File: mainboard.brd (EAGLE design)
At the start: 96.5 x 29.2 mm, 20 parts, among them IC1 LF353D, J1 AUDIO-JACKERTHENVAR, J2 AUDIO-JACKERTHENVAR, J3 AUDIO-JACKERTHENVAR, J4 AUDIO-JACKERTHENVAR, J5 AUDIO-JACKERTHENVAR, J6 POWER_SIMPLE10, P1 100KB, P2 100KB, P3 100KB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

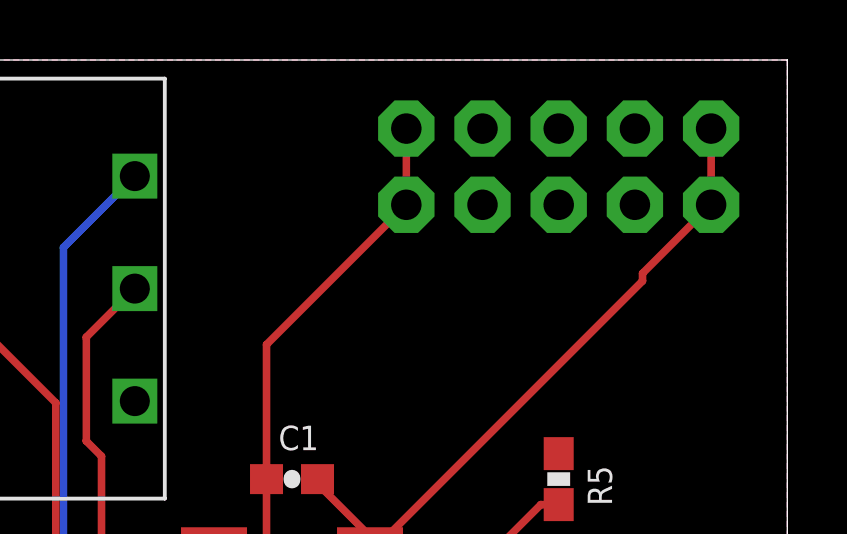
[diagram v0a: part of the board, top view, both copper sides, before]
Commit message: Switched to 16 pin connector.
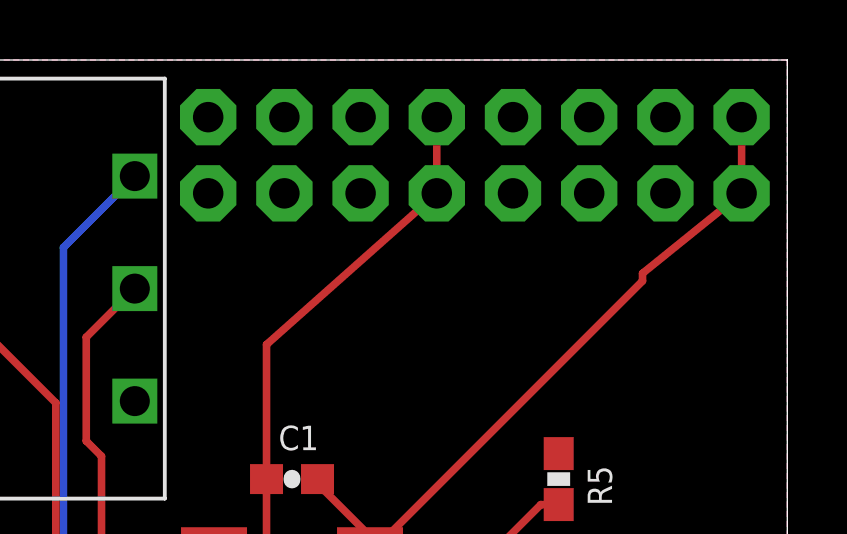
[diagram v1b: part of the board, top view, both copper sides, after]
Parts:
- J6: value POWER_SIMPLE10 -> POWER_SIMPLE16; device eurorack:POWER_10 -> eurorack:POWER_16
- moved J6 0.46 mm to (88.6, 26.0)
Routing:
- net -12V: track 21.3 -> 22.3 mm
- net +12V: track 20.8 -> 21.8 mm
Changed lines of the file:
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@@
 <attribute name="VALUE" x="81.915" y="15.367" size="1.27" layer="27" rot="R180"/>
 </element>
-<element name="J6" library="eurorack" package="POWER_10" value="POWER_SIMPLE10" x="88.9" y="25.654" smashed="yes" rot="MR0">
-<attribute name="NAME" x="85.09" y="21.209" size="1.27" layer="26" ratio="10" rot="MR0"/>
+<element name="J6" library="eurorack" package="POWER_16" value="POWER_SIMPLE16" x="88.646" y="26.035" smashed="yes" rot="MR0">
+<attribute name="NAME" x="84.836" y="21.59" size="1.27" layer="26" ratio="10" rot="MR0"/>
 </element>
 <element name="J1" library="erthenvar" package="ERTHENVAR-JACK" value="AUDIO-JACKERTHENVAR" x="7.62" y="7.62" smashed="yes" rot="R180">
@@
 <contactref element="IC1" pad="4"/>
 <contactref element="C1" pad="1"/>
-<wire x1="93.98" y1="24.384" x2="93.98" y2="26.924" width="0.254" layer="1"/>
+<wire x1="94.996" y1="24.765" x2="94.996" y2="27.305" width="0.254" layer="1"/>
 <wire x1="80.86" y1="15.24" x2="80.86" y2="15.085" width="0.254" layer="1"/>
 <wire x1="80.86" y1="15.085" x2="82.61" y2="13.335" width="0.254" layer="1"/>
@@
 <wire x1="83.185" y1="13.335" x2="91.694" y2="21.844" width="0.254" layer="1"/>
 <wire x1="91.694" y1="21.844" x2="91.694" y2="22.098" width="0.254" layer="1"/>
-<wire x1="91.694" y1="22.098" x2="93.98" y2="24.384" width="0.254" layer="1"/>
+<wire x1="91.694" y1="22.098" x2="94.996" y2="24.765" width="0.254" layer="1"/>
 </signal>
 <signal name="+12V">
@@
 <contactref element="IC1" pad="8"/>
 <contactref element="C1" pad="2"/>
-<wire x1="83.82" y1="24.384" x2="83.82" y2="26.924" width="0.254" layer="1"/>
+<wire x1="84.836" y1="24.765" x2="84.836" y2="27.305" width="0.254" layer="1"/>
 <wire x1="79.16" y1="15.24" x2="79.16" y2="10.072" width="0.254" layer="1"/>
 <wire x1="79.16" y1="10.072" x2="78.74" y2="9.652" width="0.254" layer="1"/>
@@
 <wire x1="77.537" y1="9.652" x2="77.41" y2="9.525" width="0.254" layer="1"/>
 <wire x1="79.16" y1="15.24" x2="79.16" y2="19.724" width="0.254" layer="1"/>
-<wire x1="79.16" y1="19.724" x2="83.82" y2="24.384" width="0.254" layer="1"/>
+<wire x1="79.16" y1="19.724" x2="84.836" y2="24.765" width="0.254" layer="1"/>
 </signal>
 <signal name="N$1">

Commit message: @brendan0powers helped me fix the schem/board
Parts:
- added R10: 1K, SparkFun-Resistors:0603-RES
- added R8: 51K, SparkFun-Resistors:0603-RES
- added R9: 100K, SparkFun-Resistors:0603-RES
- R7: value 1K -> 100K
- moved R6 16.2 mm to (91.4, 14.0)
- moved R7 14.3 mm to (82.5, 17.8)
- moved R1 13.0 mm to (78.7, 14.0)
- moved R2 13.0 mm to (78.7, 16.5)
- moved R3 13.0 mm to (78.7, 19.1)
- moved R4 12.5 mm to (78.7, 21.6), turned to 0 degrees
- moved C1 12.0 mm to (90.2, 21.6)
- moved IC1 12.0 mm to (90.2, 17.8)
- moved R5 6.84 mm to (95.2, 17.8), turned to 270 degrees
- moved U$1 2.54 mm to (91.2, 19.1)
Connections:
- new net N$12: IC1.7, R10.1, R9.2
- new net N$14: IC1.6, R7.2, R9.1
- new net N$15: IC1.5, R8.2
- net GND: now also R8.1; no longer IC1.5
- net N$3: now also R10.2; no longer R7.2
- net N$8: no longer IC1.6, IC1.7
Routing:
- net N$12: track 0.00 -> 14.6 mm, vias 0 -> 2
- net N$8: track 26.5 -> 15.7 mm
- net -12V: track 22.3 -> 11.8 mm
- net N$10: track 11.5 -> 3.12 mm
- net N$7: track 31.2 -> 23.2 mm
- net +12V: track 21.8 -> 16.1 mm
- net N$14: track 0.00 -> 5.11 mm
- net N$4: track 68.5 -> 63.4 mm
- net N$9: track 7.36 -> 2.57 mm
- net N$11: track 19.9 -> 23.4 mm
- net N$5: track 46.0 -> 43.3 mm
- net N$15: track 0.00 -> 2.05 mm
- net N$6: vias 0 -> 2
- net N$2: vias 0 -> 2
- net N$1: vias 0 -> 2

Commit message: fix for silkscreen
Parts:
- moved U$1 10.9 mm to (81.0, 15.2)
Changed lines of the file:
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@@
 <setting verticaltext="up"/>
 </settings>
-<grid distance="0.005" unitdist="inch" unit="inch" style="lines" multiple="1" display="yes" altdistance="0.005" altunitdist="inch" altunit="inch"/>
+<grid distance="0.05" unitdist="inch" unit="inch" style="lines" multiple="1" display="yes" altdistance="0.005" altunitdist="inch" altunit="inch"/>
 <layers>
-<layer number="1" name="Top" color="4" fill="1" visible="yes" active="yes"/>
+<layer number="1" name="Top" color="4" fill="1" visible="no" active="yes"/>
 <layer number="16" name="Bottom" color="1" fill="1" visible="yes" active="yes"/>
 <layer number="17" name="Pads" color="2" fill="1" visible="yes" active="yes"/>
@@
 <wire x1="96.52" y1="0" x2="96.52" y2="29.21" width="0" layer="20"/>
 <wire x1="96.52" y1="29.21" x2="0" y2="29.21" width="0" layer="20"/>
-<text x="15.24" y="26.416" size="1.6764" layer="22" font="vector" ratio="15" rot="MR0">Manual</text>
-<text x="15.24" y="24.13" size="1.6764" layer="22" font="vector" ratio="15" rot="MR0">Mixing</text>
-<text x="15.24" y="22.098" size="1.6764" layer="22" font="vector" ratio="15" rot="MR0">Utility</text>
-<text x="15.24" y="20.066" size="1.6764" layer="22" font="vector" ratio="15" rot="MR0">Alpha</text>
+<text x="81.28" y="9.906" size="1.6764" layer="22" font="vector" ratio="15" rot="MR0">Manual</text>
+<text x="81.28" y="7.62" size="1.6764" layer="22" font="vector" ratio="15" rot="MR0">Mixing</text>
+<text x="81.28" y="5.588" size="1.6764" layer="22" font="vector" ratio="15" rot="MR0">Utility</text>
+<text x="81.28" y="3.556" size="1.6764" layer="22" font="vector" ratio="15" rot="MR0">Alpha</text>
 </plain>
 <attributes>
@@
 <attribute name="VALUE" x="81.407" y="6.096" size="0.4064" layer="27" font="vector" rot="R270"/>
 </element>
-<element name="U$1" library="SparkFun" package="OSHW-LOGO-L" value="" x="91.186" y="19.05" rot="MR0"/>
+<element name="U$1" library="SparkFun" package="OSHW-LOGO-L" value="" x="81.026" y="15.24" rot="MR0"/>
 <element name="R7" library="SparkFun-Resistors" package="0603-RES" value="100K" x="82.55" y="17.78" rot="R90">
 <attribute name="PROD_ID" value="RES-10055" x="82.55" y="17.78" size="1.778" layer="27" font="vector" ratio="15" rot="R90" display="off"/>
